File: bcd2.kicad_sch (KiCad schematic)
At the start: 0 parts

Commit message: added decoupling caps
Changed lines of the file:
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@@
 	(paper "A4")
 	(junction
+		(at 55.88 99.06)
+		(diameter 0)
+		(color 0 0 0 0)
+	)
+	(junction
 		(at 64.77 114.935)
 		(diameter 0)
@@
 	(junction
 		(at 114.3 111.76)
-		(diameter 0)
-		(color 0 0 0 0)
-	)
-	(junction
-		(at 55.88 99.06)
 		(diameter 0)
 		(color 0 0 0 0)
@@
 	)
 	(symbol
-		(lib_id "power:VDD")
+		(lib_id "power:+3V3")
 		(at 55.88 99.06 0)
 		(unit 1)
@@
 			)
 		)
-		(property "Value" "VDD"
+		(property "Value" "+3V3"
 			(at 55.88 94.9269 0)
 			(effects
@@
 			)
 		)
-		(property "Description" "Power symbol creates a global label with name \"VDD\""
+		(property "Description" "Power symbol creates a global label with name \"+3V3\""
 			(at 55.88 99.06 0)
 			(effects

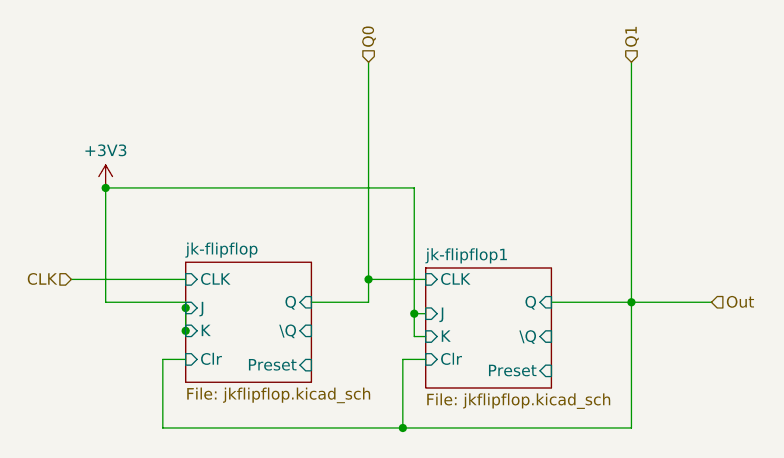
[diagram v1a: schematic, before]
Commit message: corrected output/input type of pins
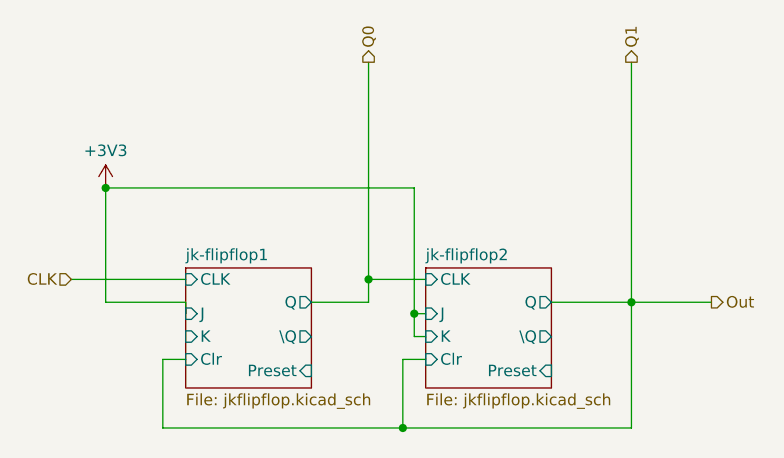
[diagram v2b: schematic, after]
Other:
- removed sheet jk-flipflop
- added sheet jk-flipflop2 (jkflipflop.kicad_sch)
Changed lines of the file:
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@@
-	)
-	(junction
-		(at 64.77 114.935)
-		(diameter 0)
-		(color 0 0 0 0)
 	)
 	(junction
@@
 		(color 0 0 0 0)
 	)
-	(junction
-		(at 64.77 112.395)
-		(diameter 0)
-		(color 0 0 0 0)
-	)
 	(wire
 		(pts
@@
 	(wire
 		(pts
-			(xy 64.77 115.57) (xy 64.77 114.935)
-		)
-		(stroke
-			(width 0)
-			(type default)
-		)
-	)
-	(wire
-		(pts
 			(xy 88.9 118.11) (xy 88.9 125.73)
 		)
@@
 	(wire
 		(pts
-			(xy 64.77 114.935) (xy 64.77 112.395)
+			(xy 64.77 111.76) (xy 64.77 113.03)
 		)
 		(stroke
@@
 	(wire
 		(pts
-			(xy 64.77 112.395) (xy 64.77 111.76)
-		)
-		(stroke
-			(width 0)
-			(type default)
-		)
-	)
-	(wire
-		(pts
 			(xy 105.41 111.76) (xy 114.3 111.76)
 		)
@@
 	)
 	(hierarchical_label "Q1"
-		(shape input)
+		(shape output)
 		(at 114.3 85.09 90)
 		(effects
@@
 	)
 	(hierarchical_label "Out"
-		(shape input)
+		(shape output)
 		(at 123.19 111.76 0)
 		(effects
@@
 	)
 	(hierarchical_label "Q0"
-		(shape input)
+		(shape output)
 		(at 85.09 85.09 90)
 		(effects
@@
 		(dnp no)
 		(fields_autoplaced yes)
-		(property "Reference" "#PWR057"
+		(property "Reference" "#PWR0175"
 			(at 55.88 102.87 0)
 			(effects
@@
 			(project "transistor-clock"
 				(path "/ce10d5bc-995e-4952-aa76-0a08f713a0f2/2c36a9e9-de42-4705-9ad4-94f4cc168e2f/e5d5ceff-c3df-4aeb-b3ac-c735ee65b6d1"
-					(reference "#PWR057")
+					(reference "#PWR0175")
 					(unit 1)
 				)
@@
 	)
 	(sheet
-		(at 64.77 107.315)
+		(at 64.77 107.95)
 		(size 13.97 13.335)
 		(exclude_from_sim no)
@@
 			(color 255 255 255 0.0000)
 		)
-		(property "Sheetname" "jk-flipflop"
-			(at 64.77 106.6034 0)
+		(property "Sheetname" "jk-flipflop1"
+			(at 64.77 107.2384 0)
 			(effects
 				(font
@@
 		)
 		(property "Sheetfile" "jkflipflop.kicad_sch"
-			(at 64.77 121.2346 0)
+			(at 64.77 121.8696 0)
 			(effects
 				(font
@@
 		)
 		(pin "J" input
-			(at 64.77 112.395 180)
+			(at 64.77 113.03 180)
 			(effects
 				(font
@@
 		)
 		(pin "K" input
-			(at 64.77 114.935 180)
+			(at 64.77 115.57 180)
 			(effects
 				(font
@@
 		)
 		(pin "Preset" input
-			(at 78.74 118.745 0)
+			(at 78.74 119.38 0)
 			(effects
 				(font
@@
 			)
 		)
-		(pin "Q" input
+		(pin "Q" output
 			(at 78.74 111.76 0)
 			(effects
@@
 			)
 		)
-		(pin "\\Q" input
-			(at 78.74 114.935 0)
+		(pin "\\Q" output
+			(at 78.74 115.57 0)
 			(effects
 				(font
@@
 			(project "transistor-clock"
 				(path "/ce10d5bc-995e-4952-aa76-0a08f713a0f2/2c36a9e9-de42-4705-9ad4-94f4cc168e2f/e5d5ceff-c3df-4aeb-b3ac-c735ee65b6d1"
-					(page "138")
+					(page "122")
 				)
 			)
@@
 			(color 255 255 255 0.0000)
 		)
-		(property "Sheetname" "jk-flipflop1"
+		(property "Sheetname" "jk-flipflop2"
 			(at 91.44 107.2384 0)
 			(effects
@@
 			)
 		)
-		(pin "Q" input
+		(pin "Q" output
 			(at 105.41 111.76 0)
 			(effects
@@
 			)
 		)
-		(pin "\\Q" input
+		(pin "\\Q" output
 			(at 105.41 115.57 0)
 			(effects
@@
 			(project "transistor-clock"
 				(path "/ce10d5bc-995e-4952-aa76-0a08f713a0f2/2c36a9e9-de42-4705-9ad4-94f4cc168e2f/e5d5ceff-c3df-4aeb-b3ac-c735ee65b6d1"
-					(page "146")
-				)
-			)
+					(page "127")
+				)
+			)

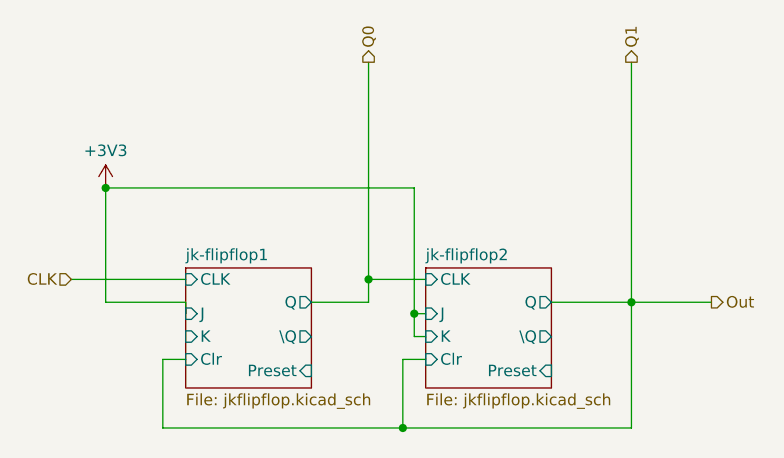
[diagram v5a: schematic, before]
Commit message: switched to using flipflop module
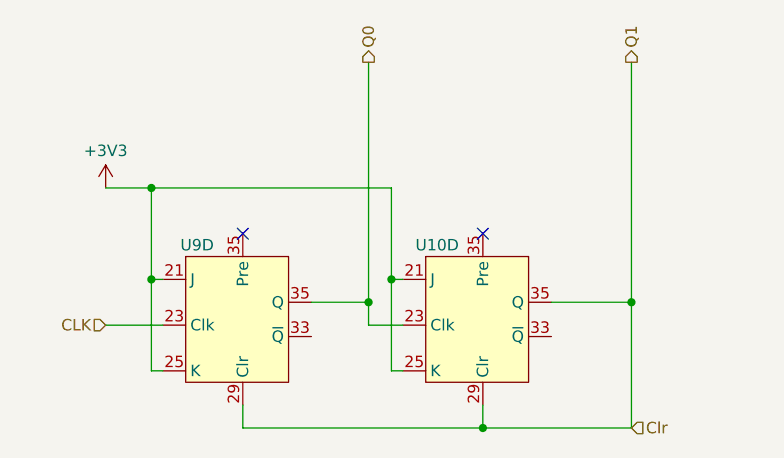
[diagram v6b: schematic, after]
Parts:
- added U10, U9: ~, symbol custom:jk-flipflops
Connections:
- net +3V3: now also U10.21 (J), U10.25 (K), U9.21 (J), U9.25 (K)
- net CLK: now also U9.23 (Clk)
- net Q0: now also U10.23 (Clk), U9.35 (Q)
- new net Clr: U10.29 (Clr), U10.35 (Q), U9.29 (Clr)
- no-connect marks 0 -> 2
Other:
- removed sheet jk-flipflop1
- removed sheet jk-flipflop2
